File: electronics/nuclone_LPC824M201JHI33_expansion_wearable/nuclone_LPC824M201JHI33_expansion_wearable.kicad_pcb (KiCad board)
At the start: 2 copper layers, 48.3 x 48.3 mm, 11 parts, among them J1 nuclone_small_left, J2 nuclone_small_right, J3 PINS_1X18, J4 PINS_1X17

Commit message: WIP PCB preparation for labeling
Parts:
- removed J3: PINS_1X18, SquantorConnectors:Header-0127-1X18-H006
- removed J4: PINS_1X17, SquantorConnectors:Header-0127-1X17-H006
- N2: value 20200808 -> 20200910
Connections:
- J1 pad 1: /VDD1 -> /VDD
- J1 pad 10: /GPIO_03 -> /PIO0_4
- J1 pad 11: /GPIO_04 -> /PIO0_28
- J1 pad 12: /GPIO_05 -> /PIO0_3
- J1 pad 13: /GPIO_06 -> /PIO0_2
- J1 pad 14: /GPIO_07 -> /PIO0_11
- J1 pad 15: /GPIO_08 -> /PIO0_10
- J1 pad 16: /GPIO_09 -> /PIO0_16
- J1 pad 17: /GPIO_10 -> /PIO0_27
- J1 pad 18: /GPIO_11 -> /PIO0_26
- J1 pad 19: /GPIO_12 -> /PIO0_25
- J1 pad 2: /VDD1 -> /VDD
- J1 pad 20: /GPIO_13 -> /PIO0_24
- J1 pad 5: /VSS1 -> /VSS
- J1 pad 6: /VSS1 -> /VSS
- J1 pad 7: /GPIO_00 -> /PIO0_13
- J1 pad 8: /GPIO_01 -> /PIO0_12
- J1 pad 9: /GPIO_02 -> /PIO0_5
- J2 pad 1: /GPIO_14 -> Net-(J2-Pad1)
- J2 pad 10: /GPIO_23 -> /PIO0_14
- J2 pad 11: /GPIO_24 -> /PIO0_21
- J2 pad 12: /GPIO_25 -> /PIO0_22
- J2 pad 13: /GPIO_26 -> /PIO0_19
- J2 pad 14: /GPIO_27 -> /PIO0_20
- J2 pad 15: /GPIO_28 -> /PIO0_17
- J2 pad 16: /GPIO_29 -> /PIO0_18
- J2 pad 17: /VSS2 -> /VSS
- J2 pad 18: /VSS2 -> /VSS
- J2 pad 19: /VDD2 -> /VDD
- J2 pad 2: /GPIO_15 -> Net-(J2-Pad2)
- J2 pad 20: /VDD2 -> /VDD
- J2 pad 3: /GPIO_16 -> /PIO0_8
- J2 pad 4: /GPIO_17 -> /PIO0_9
- J2 pad 5: /GPIO_18 -> /PIO0_7
- J2 pad 6: /GPIO_19 -> Net-(J2-Pad6)
- J2 pad 7: /GPIO_20 -> /PIO0_0
- J2 pad 8: /GPIO_21 -> /PIO0_6
- J2 pad 9: /GPIO_22 -> /PIO0_23
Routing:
- net /GPIO_22: track 7.67 -> 0.00 mm
- net /GPIO_18: track 7.67 -> 0.00 mm
- net /GPIO_28: track 7.67 -> 0.00 mm
- net /GPIO_24: track 7.67 -> 0.00 mm
- net /GPIO_20: track 7.67 -> 0.00 mm
- net /GPIO_16: track 7.67 -> 0.00 mm
- net /GPIO_26: track 7.67 -> 0.00 mm
- net /VDD1: track 7.51 -> 0.00 mm
- net /GPIO_12: track 7.40 -> 0.00 mm
- net /GPIO_10: track 7.40 -> 0.00 mm
- net /GPIO_06: track 7.40 -> 0.00 mm
- net /GPIO_02: track 7.40 -> 0.00 mm
- net /GPIO_08: track 7.40 -> 0.00 mm
- net /GPIO_04: track 7.40 -> 0.00 mm
- net /GPIO_00: track 7.40 -> 0.00 mm
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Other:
- board text added: "PIO0_12"
- board text added: "PIO0_13"
- board text added: "PIO0_2"
- board text added: "PIO0_28"
- board text added: "PIO0_3"
- board text added: "PIO0_4"
- board text added: "PIO0_5"
- board text removed: "GPIO00"
- board text removed: "GPIO01"
- board text removed: "GPIO02"
- board text removed: "GPIO03"
- board text removed: "GPIO04"
- board text removed: "GPIO05"
- board text removed: "GPIO06"

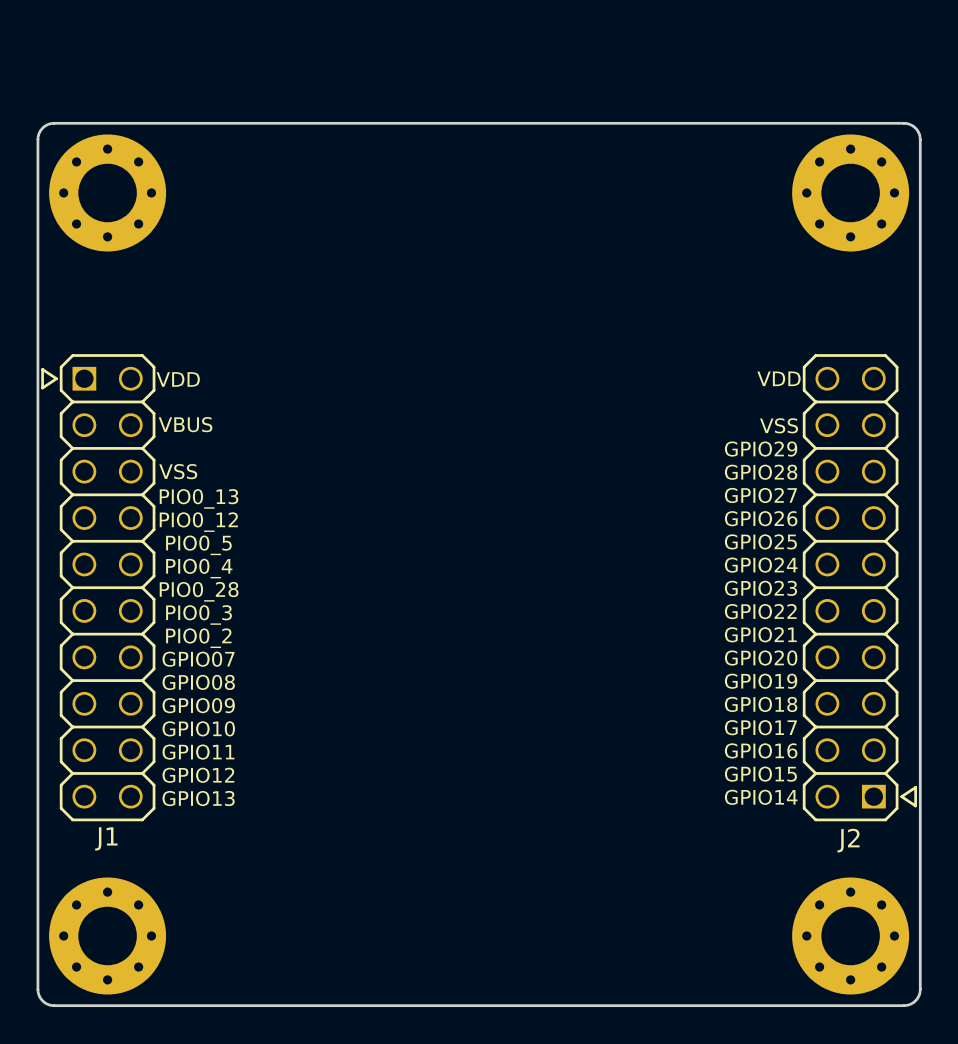
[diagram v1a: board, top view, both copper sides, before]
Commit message: completed labeling, nice point to make a template out of it
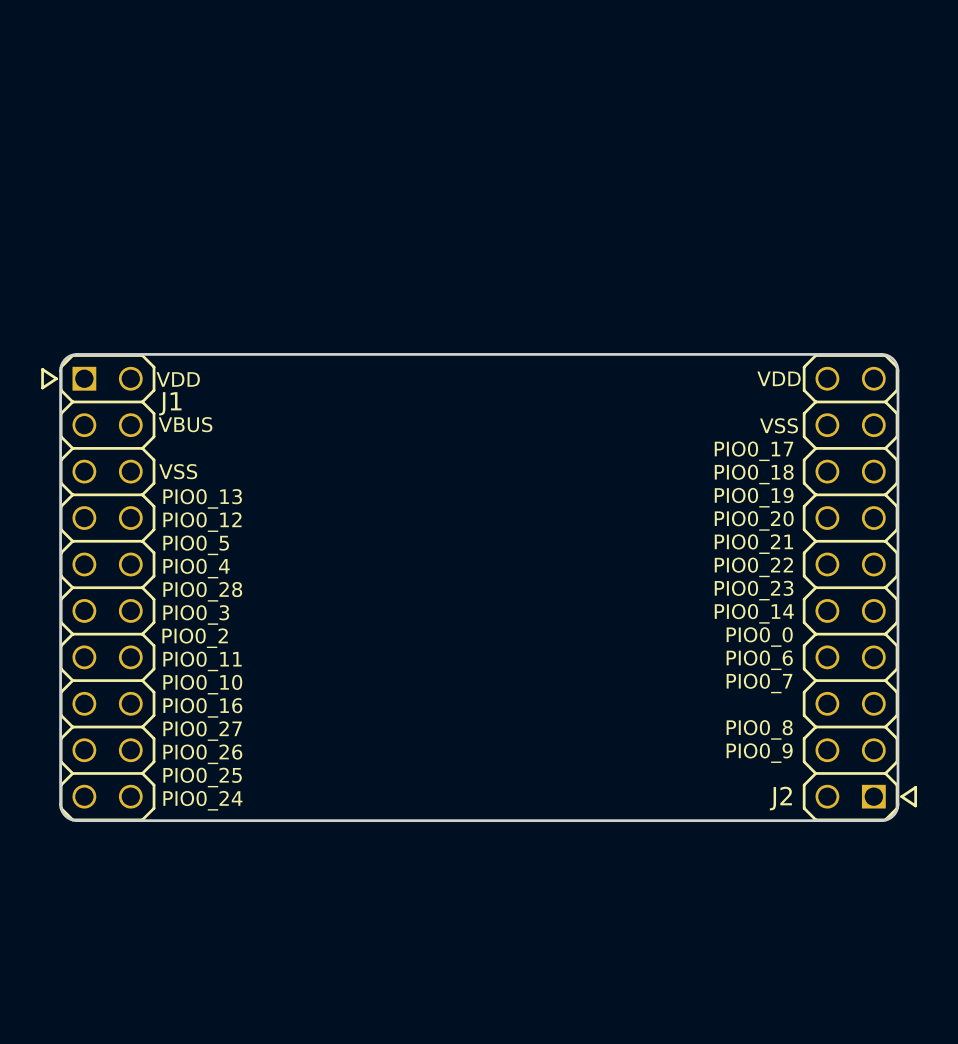
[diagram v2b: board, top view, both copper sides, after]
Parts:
- removed H1, H2, H3, H4: MountingHole, MountingHole:MountingHole_3.2mm_M3_Pad_Via
- moved N1 9.90 mm to (85.4, 92.0)
- moved N2 9.90 mm to (83.9, 96.0)
- moved N3 9.90 mm to (86.2, 98.0)
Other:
- board size 48.3 x 48.3 mm -> 45.8 x 25.5 mm
- board text added: "PIO0_0"
- board text added: "PIO0_10"
- board text added: "PIO0_11"
- board text added: "PIO0_14"
- board text added: "PIO0_16"
- board text added: "PIO0_17"
- board text added: "PIO0_18"
- board text added: "PIO0_19"
- board text added: "PIO0_20"
- board text added: "PIO0_21"
- board text added: "PIO0_22"
- board text added: "PIO0_23"
- board text added: "PIO0_24"
- board text added: "PIO0_25"
- board text added: "PIO0_26"
- board text added: "PIO0_27"
- board text added: "PIO0_6"
- board text added: "PIO0_7"
- board text added: "PIO0_8"
- board text added: "PIO0_9"
- board text removed: "GPIO07"
- board text removed: "GPIO08"
- board text removed: "GPIO09"
- board text removed: "GPIO10"
- board text removed: "GPIO11"
- board text removed: "GPIO12"
- board text removed: "GPIO13"
- board text removed: "GPIO14"
- board text removed: "GPIO15"
- board text removed: "GPIO16"
- board text removed: "GPIO17"
- board text removed: "GPIO18"
- board text removed: "GPIO19"
- board text removed: "GPIO20"
- board text removed: "GPIO21"
- board text removed: "GPIO22"
- board text removed: "GPIO23"
- board text removed: "GPIO24"
- board text removed: "GPIO25"
- board text removed: "GPIO26"
- board text removed: "GPIO27"
- board text removed: "GPIO28"
- board text removed: "GPIO29"

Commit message: added UART connection, layed out and routed
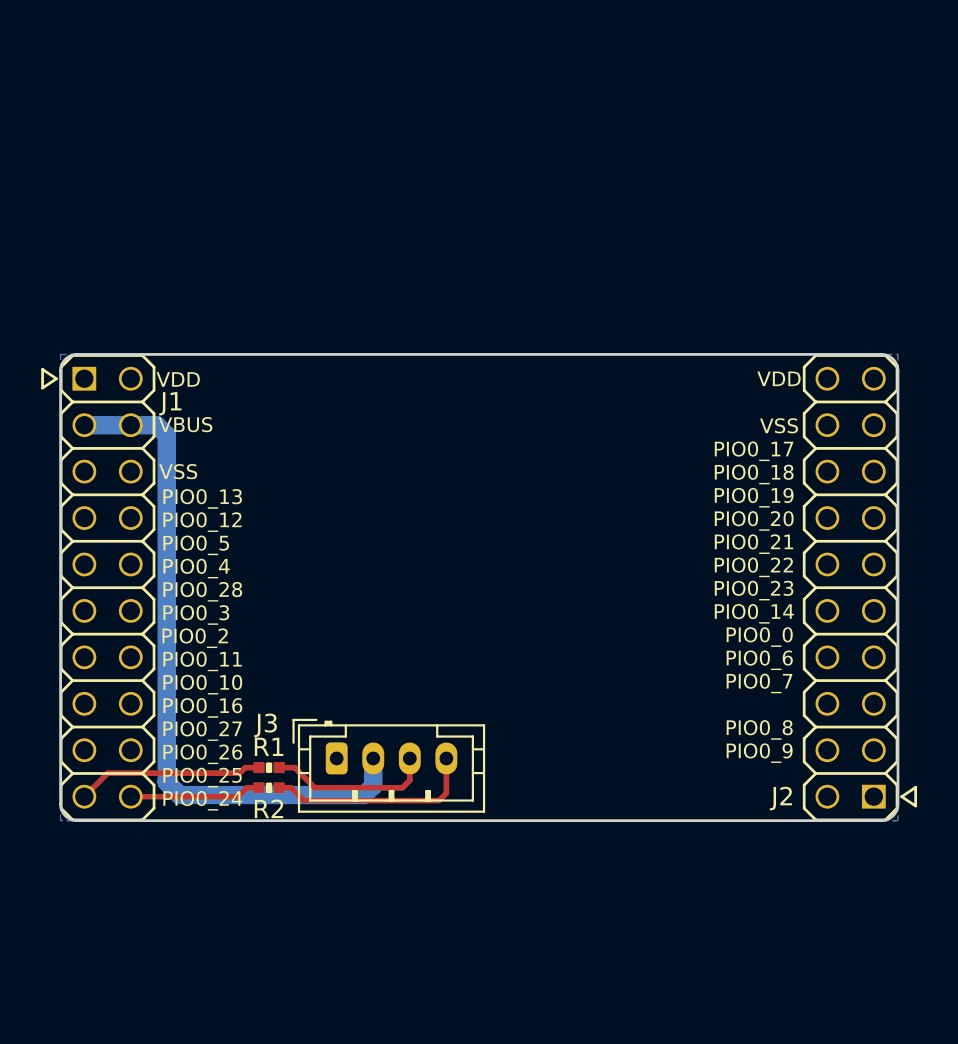
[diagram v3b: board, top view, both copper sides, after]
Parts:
- added J3: DevBoardUartInput, Connector_JST:JST_PH_B4B-PH-K_1x04_P2.00mm_Vertical, F.Cu at (77.3, 95.7)
- added R1: 100, SquantorRcl:R_0402_hand, F.Cu at (73.6, 96.2)
- added R2: 100, SquantorRcl:R_0402_hand, F.Cu at (73.6, 97.3)
- moved N1 34.8 mm to (119.4, 84.5)
- moved N2 34.8 mm to (117.9, 88.5)
- moved N3 34.8 mm to (120.2, 90.5)
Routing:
- net /VBUS: track 0.00 -> 37.0 mm
- net Net-(J3-Pad4): track 0.00 -> 11.5 mm
- net /PIO0_25: track 0.00 -> 10.2 mm
- net Net-(J3-Pad3): track 0.00 -> 8.97 mm
- net /PIO0_24: track 0.00 -> 7.21 mm
- added copper zone on B.Cu, net /VSS

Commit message: imported some components
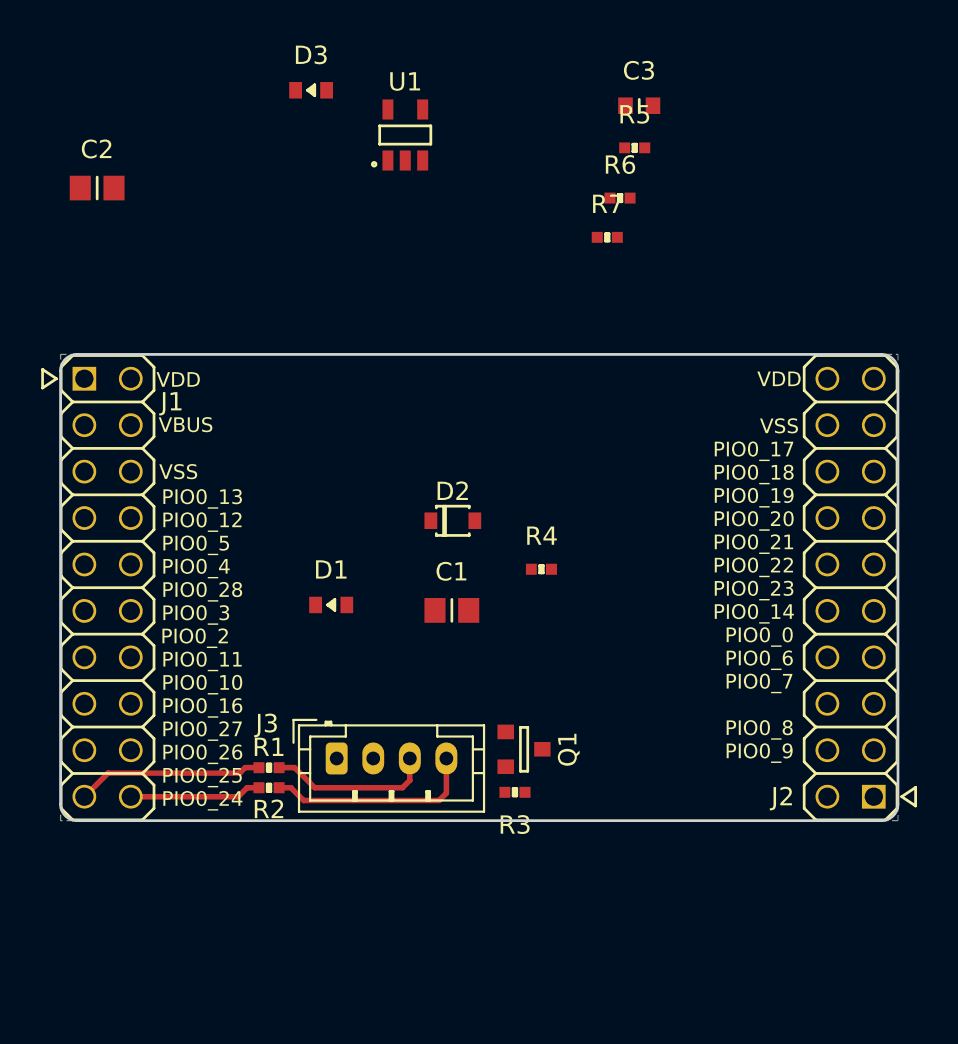
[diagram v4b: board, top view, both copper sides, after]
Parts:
- added C1: 10u, SquantorRcl:C_0805+0603, F.Cu at (83.6, 87.6)
- added C2: 10u, SquantorRcl:C_0805+0603, F.Cu at (64.2, 64.5)
- added C3: 1u, SquantorRcl:C_0603, F.Cu at (93.8, 60.0)
- added D1: GRN, SquantorDiodes:LED_0603_hand, F.Cu at (77.0, 87.3)
- added D2: NSR0320, SquantorDiodes:SOD_323_onsemi, F.Cu at (83.7, 82.7)
- added D3: RED, SquantorDiodes:LED_0603_hand, F.Cu at (75.9, 59.1)
- added Q1: DMG2305, SquantorIC:SOT23-3, F.Cu at (87.5, 95.2)
- added R3: 100K, SquantorRcl:R_0402_hand, F.Cu at (87.0, 97.5)
- added R4: 1K, SquantorRcl:R_0402_hand, F.Cu at (88.5, 85.3)
- added R5: 22K, SquantorRcl:R_0402_hand, F.Cu at (93.6, 62.3)
- added R6: 1K, SquantorRcl:R_0402_hand, F.Cu at (92.8, 65.0)
- added R7: 47K, SquantorRcl:R_0402_hand, F.Cu at (92.1, 67.2)
- added U1: MCP738312-OT, SquantorIC:SOT23-5-Microchip-OT, F.Cu at (81.0, 61.6)
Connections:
- J3 pad 2: /VBUS -> /VUSB
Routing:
- net /VBUS: track 37.0 -> 0.00 mm
